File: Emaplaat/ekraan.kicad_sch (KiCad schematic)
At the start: 0 parts

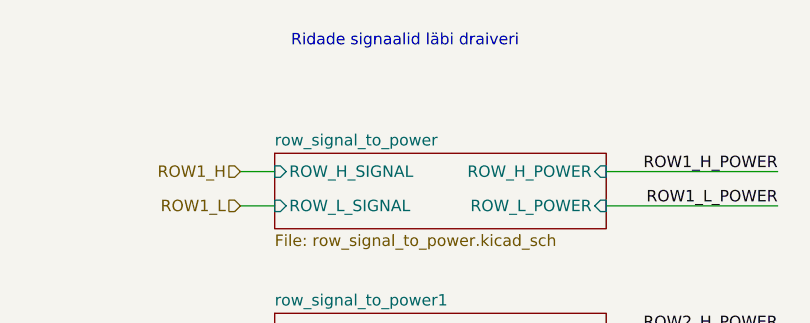
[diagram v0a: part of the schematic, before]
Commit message: 3V3 voolud kontrollitud
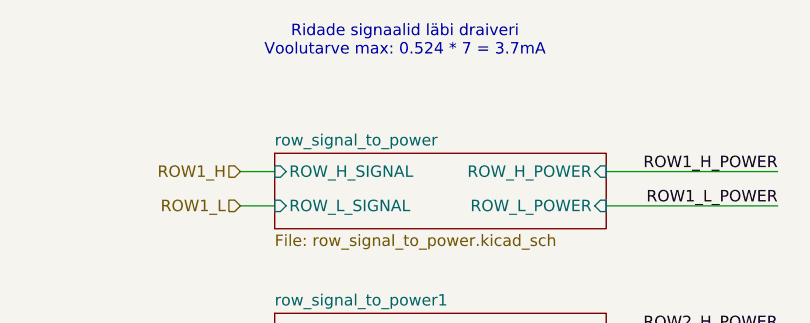
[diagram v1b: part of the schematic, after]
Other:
- note added: "Ridade signaalid läbi draiveri Voolutarve max: 0.524 * 7 = 3.7mA"
- note removed: "Ridade signaalid läbi draiveri"
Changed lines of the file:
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@@
 		)
 	)
-	(text "Ridade signaalid läbi draiveri"
+	(text "Ridade signaalid läbi draiveri\nVoolutarve max: 0.524 * 7 = 3.7mA"
 		(exclude_from_sim no)
 		(at 143.764 21.082 0)

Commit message: jajald
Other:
- note added: "Ridade signaalid läbi draiveri Voolutarve max: 0.524 * 7 = 3.7mA 14 draiverit veerugdele 14mA 12V-st"
- note added: "Veergude signaalid läbi draiveri 14 column driverit võtavad 14mA kokku kõik 12V-st"
- note removed: "Ridade signaalid läbi draiveri Voolutarve max: 0.524 * 7 = 3.7mA"
- note removed: "Veergude signaalid läbi draiveri"
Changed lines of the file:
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@@
 		)
 	)
-	(text "Veergude signaalid läbi draiveri"
+	(text "Veergude signaalid läbi draiveri\n14 column driverit võtavad 14mA kokku kõik 12V-st"
 		(exclude_from_sim no)
 		(at 61.976 54.61 0)
@@
 		)
 	)
-	(text "Ridade signaalid läbi draiveri\nVoolutarve max: 0.524 * 7 = 3.7mA"
+	(text "Ridade signaalid läbi draiveri\nVoolutarve max: 0.524 * 7 = 3.7mA\n14 draiverit veerugdele 14mA 12V-st"
 		(exclude_from_sim no)
 		(at 143.764 21.082 0)

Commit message: v2.3 VALMIS
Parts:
- added H2, H3, H4: MountingHole, MountingHole:MountingHole_3mm_Pad, symbol Mechanical:MountingHole
- added TP1, TP10, TP11, TP12, TP13, TP14, TP15, TP16, TP17, TP18, TP19, TP2, TP20, TP21, TP22, TP23, TP24, TP25, TP26, TP27, TP28, TP3, TP4, TP5, TP6, TP7, TP8, TP9: TestPoint, TestPoint:TestPoint_Pad_D1.0mm, symbol Connector:TestPoint
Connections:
- net COLUMN10_POWER: now also TP5.1
- net COLUMN11_POWER: now also TP4.1
- net COLUMN12_POWER: now also TP3.1
- net COLUMN13_POWER: now also TP2.1
- net COLUMN14_POWER: now also TP1.1
- net COLUMN1_POWER: now also TP14.1
- net COLUMN2_POWER: now also TP13.1
- net COLUMN3_POWER: now also TP12.1
- net COLUMN4_POWER: now also TP11.1
- net COLUMN5_POWER: now also TP10.1
- net COLUMN6_POWER: now also TP9.1
- net COLUMN7_POWER: now also TP8.1
- net COLUMN8_POWER: now also TP7.1
- net COLUMN9_POWER: now also TP6.1
- net ROW1_H_POWER: now also TP28.1
- net ROW1_L_POWER: now also TP27.1
- net ROW2_H_POWER: now also TP26.1
- net ROW2_L_POWER: now also TP25.1
- net ROW3_H_POWER: now also TP24.1
- net ROW3_L_POWER: now also TP23.1
- net ROW4_H_POWER: now also TP22.1
- net ROW4_L_POWER: now also TP21.1
- net ROW5_H_POWER: now also TP20.1
- net ROW5_L_POWER: now also TP19.1
- net ROW6_H_POWER: now also TP18.1
- net ROW6_L_POWER: now also TP17.1
- net ROW7_H_POWER: now also TP16.1
- net ROW7_L_POWER: now also TP15.1
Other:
- note added: "testpad-id kontrollimiseks"
